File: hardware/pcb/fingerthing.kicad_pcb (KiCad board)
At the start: 2 copper layers, 52 x 51 mm, 43 parts, among them J1 10103594-0001LF, J2 TSW-118-07-L-D, J3 TSW-118-07-L-D, J4 SM03B-SRSS-TB(LF)(SN), SW1 434133025816, SW2 434133025816, U1 RP2350A, U2 NCP1117ST33T3G, U3 W25Q128JVSIQ, X1 12MHz

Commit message: usb / sensor layout
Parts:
- removed J3: TSW-118-07-L-D, RPI_COMPILED:samtec_tsw-118-07-l-d
- removed R4: 1k, RPI_COMPILED:generic_resc1005x35
- removed R9: 0, RPI_COMPILED:generic_resc1005x35
- removed SW2: 434133025816, RPI_COMPILED:wurthelek_434133025816
- added D1: green, LED_SMD:LED_0603_1608Metric, F.Cu at (30.0, 24.0)
- added R11: 5.1k, Resistor_SMD:R_0402_1005Metric, F.Cu at (10.5, 8.50)
- added R12: 5.1k, Resistor_SMD:R_0402_1005Metric, F.Cu at (23.5, 9.50)
- added R13: 1k, Resistor_SMD:R_0402_1005Metric, F.Cu at (30.0, 26.0)
- added R14: 10k, Resistor_SMD:R_0402_1005Metric, F.Cu at (10.0, 39.0)
- added SW3: 434133025816, RPI_COMPILED:wurthelek_434133025816, F.Cu at (10.0, 43.0)
- added U4: USBLC6-2SC6, Package_TO_SOT_SMD:SOT-23-6, F.Cu at (17.0, 11.0)
- J1: value 10103594-0001LF -> USB4105-GF-A; footprint RPI_COMPILED:amphenol_10103594-0001lf -> Connector_USB:USB_C_Receptacle_GCT_USB4105-xx-A_16P_TopMnt_Horizontal
- J2: value TSW-118-07-L-D -> R503; footprint RPI_COMPILED:samtec_tsw-118-07-l-d -> Connector_JST:JST_SH_SM06B-SRSS-TB_1x06-1MP_P1.00mm_Horizontal; moved to B.Cu
- J4: moved to B.Cu
- moved J4 112.5 mm to (25.5, 38.5), turned to 180 degrees
- moved MH3 111.0 mm to (30.5, 44.0)
- moved MH4 110.3 mm to (3.50, 44.0)
- moved C10 109.9 mm to (17.8, 34.9)
- moved C11 109.9 mm to (24.1, 27.4)
- moved C12 109.9 mm to (14.9, 20.6)
- moved C13 109.9 mm to (10.5, 24.6)
- moved C14 109.9 mm to (24.1, 28.4)
- moved C15 109.9 mm to (10.5, 29.4)
- moved C16 109.9 mm to (22.7, 32.0)
- moved C17 109.9 mm to (23.5, 25.0)
- moved C18 109.9 mm to (15.2, 34.1)
- moved C2 109.9 mm to (13.2, 10.8)
- moved C3 109.9 mm to (15.6, 37.0)
- moved C4 109.9 mm to (18.6, 37.0)
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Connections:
- net +1V1 renamed /+1V1
- net Net-(U1-USB_DM) renamed /USB_DM
- net Net-(U1-USB_DP) renamed /USB_DP
- C1 pad 1: VBUS -> /VBUS
- C1 pad 2: GND -> /GND
- C10 pad 2: GND -> /GND
- C11 pad 2: GND -> /GND
- C12 pad 1: +3V3 -> /+3V3
- C12 pad 2: GND -> /GND
- C13 pad 1: +3V3 -> /+3V3
- C13 pad 2: GND -> /GND
- C14 pad 1: +3V3 -> /+3V3
- C14 pad 2: GND -> /GND
- C15 pad 1: +3V3 -> /+3V3
- C15 pad 2: GND -> /GND
- C16 pad 1: +3V3 -> /+3V3
- C16 pad 2: GND -> /GND
- C17 pad 1: +3V3 -> /+3V3
- C17 pad 2: GND -> /GND
- C18 pad 1: +3V3 -> /+3V3
- C18 pad 2: GND -> /GND
- C19 pad 1: +3V3 -> /+3V3
- C19 pad 2: GND -> /GND
- C2 pad 1: +3V3 -> /+3V3
- C2 pad 2: GND -> /GND
- C3 pad 2: GND -> /GND
- C4 pad 2: GND -> /GND
- C5 pad 1: +3V3 -> /+3V3
- C5 pad 2: GND -> /GND
- C6 pad 1: +3V3 -> /+3V3
- C6 pad 2: GND -> /GND
- C7 pad 2: GND -> /GND
- C8 pad 2: GND -> /GND
- C9 pad 2: GND -> /GND
- J2 pad 1: GND -> /+3V3
- J2 pad 2: +3V3 -> /GND
- J2 pad 3: GND -> /GPIO5
- J2 pad 4: /GPIO0 -> /GPIO4
- J2 pad 5: GND -> /GPIO7
- J2 pad 6: /GPIO1 -> /+3V3
- J4 pad 2: GND -> /GND
- J4 pad 4: GND -> /GND
- J4 pad 5: GND -> /GND
- R1 pad 1: +3V3 -> /+3V3
- R3 pad 1: +3V3 -> /+3V3
- SW1 pad 1: GND -> /GND
- SW1 pad 2: GND -> /GND
- U1 pad 1: +3V3 -> /+3V3
- U1 pad 11: +3V3 -> /+3V3
- U1 pad 12: /GPIO8 -> unconnected-(U1-GPIO8-Pad12)
- U1 pad 13: /GPIO9 -> unconnected-(U1-GPIO9-Pad13)
- U1 pad 14: /GPIO10 -> unconnected-(U1-GPIO10-Pad14)
- U1 pad 15: /GPIO11 -> unconnected-(U1-GPIO11-Pad15)
- U1 pad 16: /GPIO12 -> unconnected-(U1-GPIO12-Pad16)
- U1 pad 17: /GPIO13 -> unconnected-(U1-GPIO13-Pad17)
- U1 pad 18: /GPIO14 -> unconnected-(U1-GPIO14-Pad18)
- U1 pad 19: /GPIO15 -> unconnected-(U1-GPIO15-Pad19)
- U1 pad 2: /GPIO0 -> unconnected-(U1-GPIO0-Pad2)
- U1 pad 20: +3V3 -> /+3V3
- U1 pad 26: /RUN -> unconnected-(U1-RUN-Pad26)
- U1 pad 27: /GPIO16 -> unconnected-(U1-GPIO16-Pad27)
- U1 pad 28: /GPIO17 -> unconnected-(U1-GPIO17-Pad28)
- U1 pad 29: /GPIO18 -> unconnected-(U1-GPIO18-Pad29)
- U1 pad 3: /GPIO1 -> unconnected-(U1-GPIO1-Pad3)
- U1 pad 30: +3V3 -> /+3V3
- U1 pad 31: /GPIO19 -> unconnected-(U1-GPIO19-Pad31)
- U1 pad 32: /GPIO20 -> unconnected-(U1-GPIO20-Pad32)
- U1 pad 33: /GPIO21 -> unconnected-(U1-GPIO21-Pad33)
- U1 pad 34: /GPIO22 -> unconnected-(U1-GPIO22-Pad34)
- U1 pad 35: /GPIO23 -> unconnected-(U1-GPIO23-Pad35)
- U1 pad 36: /GPIO24 -> unconnected-(U1-GPIO24-Pad36)
- U1 pad 38: +3V3 -> /+3V3
- U1 pad 4: /GPIO2 -> unconnected-(U1-GPIO2-Pad4)
- U1 pad 40: /GPIO26_ADC0 -> unconnected-(U1-GPIO26_ADC0-Pad40)
- U1 pad 41: /GPIO27_ADC1 -> unconnected-(U1-GPIO27_ADC1-Pad41)
- U1 pad 42: /GPIO28_ADC2 -> unconnected-(U1-GPIO28_ADC2-Pad42)
- U1 pad 43: /GPIO29_ADC3 -> unconnected-(U1-GPIO29_ADC3-Pad43)
- U1 pad 44: +3V3 -> /+3V3
- U1 pad 45: +3V3 -> /+3V3
- U1 pad 47: GND -> /GND
- U1 pad 49: +3V3 -> /+3V3
- U1 pad 5: /GPIO3 -> unconnected-(U1-GPIO3-Pad5)
- U1 pad 53: +3V3 -> /+3V3
- U1 pad 54: +3V3 -> /+3V3
- U1 pad 61: GND -> /GND
- U2 pad 1: GND -> /GND
- U2 pad 2: +3V3 -> /+3V3
- U2 pad 3: VBUS -> /VBUS
- U2 pad 4: +3V3 -> /+3V3
- U3 pad 4: GND -> /GND
- U3 pad 8: +3V3 -> /+3V3
- X1 pad 2: GND -> /GND
- X1 pad 4: GND -> /GND
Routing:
- net /GPIO0: track 39.0 -> 0.00 mm, vias 2 -> 0
- net +3V3: track 37.6 -> 0.00 mm, vias 2 -> 0
- net GND: track 37.5 -> 0.00 mm, vias 27 -> 0
- net /GPIO29_ADC3: track 33.6 -> 0.00 mm
- net /GPIO28_ADC2: track 31.9 -> 0.00 mm
- net /GPIO27_ADC1: track 30.3 -> 0.00 mm
- net /GPIO1: track 29.8 -> 0.00 mm
- net /GPIO26_ADC0: track 28.6 -> 0.00 mm
- net /GPIO2: track 28.2 -> 0.00 mm
- net /SWCLK: track 27.8 -> 0.00 mm
- net /GPIO25: track 27.7 -> 0.00 mm
- net /GPIO3: track 26.5 -> 0.00 mm
- net /GPIO24: track 26.1 -> 0.00 mm
- net /SWD: track 25.4 -> 0.00 mm
- net /GPIO15: track 25.2 -> 0.00 mm
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- added copper zone on F.Cu, net /+3V3
- added copper zone on F.Cu, net /GND
- removed copper zone on F.Cu, net +3V3
- removed copper zone on B.Cu, net GND
- removed copper zone on F.Cu, net GND
- removed copper zone on F.Cu, net VBUS
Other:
- board size 52 x 51 mm -> 34 x 48 mm
- copper layers 2 -> 4
- board text added: "CLK GND SWD"
- board text added: "fingerthing"
- board text removed: "3V3"
- board text removed: "ADC 26-29"
- board text removed: "BOOTSEL"
- board text removed: "DEBUG"
- board text removed: "GND"
- board text removed: "GP0"
- board text removed: "GP1"
- board text removed: "GP10"
- board text removed: "GP11"
- board text removed: "GP12"
- board text removed: "GP13"
- board text removed: "GP14"
- board text removed: "GP15"
- board text removed: "GP16"
- board text removed: "GP17"
- board text removed: "GP18"
- board text removed: "GP19"
- board text removed: "GP2"
- board text removed: "GP20"
- board text removed: "GP21"
- board text removed: "GP22"
- board text removed: "GP23"
- board text removed: "GP24"
- board text removed: "GP25"
- board text removed: "GP26"
- board text removed: "GP27"
- board text removed: "GP28"
- board text removed: "GP29"
- board text removed: "GP3"
- board text removed: "GP4"
- board text removed: "GP5"
- board text removed: "GP6"
- board text removed: "GP7"
- board text removed: "GP8"
- board text removed: "GP9"
- board text removed: "Minimal Design Example R4"
- board text removed: "Outer Row GND"
- board text removed: "RUN"
- board text removed: "Raspberry Pi RP2350A QFN-60"
- board text removed: "SWCLK"
- board text removed: "SWD"

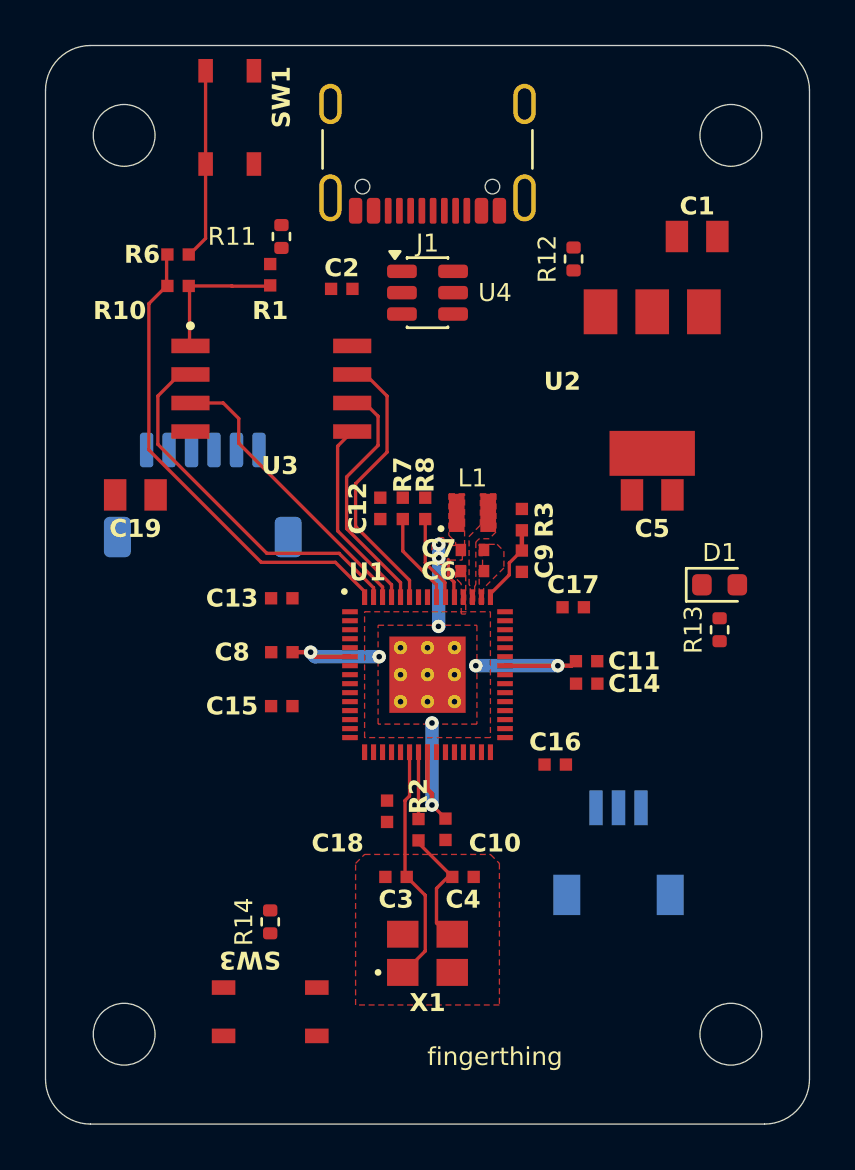
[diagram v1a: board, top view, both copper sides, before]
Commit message: pcb power / usb footprint
Ground and 3.3 V routing pass DRC clearance checks. ERC and schematic parity pass. 24 unconnected items remain.
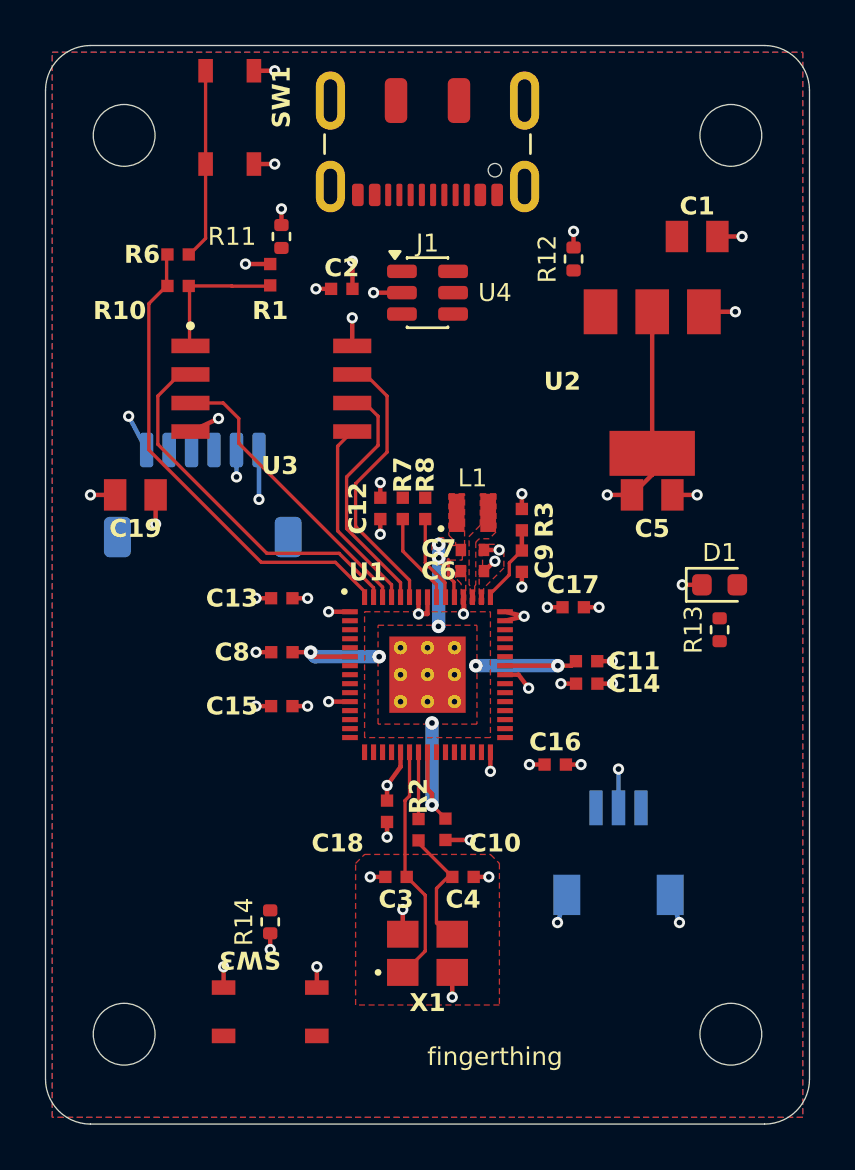
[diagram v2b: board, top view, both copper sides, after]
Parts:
- J1: value USB4105-GF-A -> DX07S016JA1R1500; footprint Connector_USB:USB_C_Receptacle_GCT_USB4105-xx-A_16P_TopMnt_Horizontal -> fingerthing:usb-c
- moved J1 0.07 mm to (17.0, 3.60)
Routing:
- net /+3V3: track 0.00 -> 35.4 mm, vias 0 -> 23
- net /GND: track 0.00 -> 32.5 mm, vias 0 -> 35
- added copper zone on In2.Cu, net /+3V3
- added copper zone on B.Cu, net /GND
- added copper zone on In1.Cu, net /GND

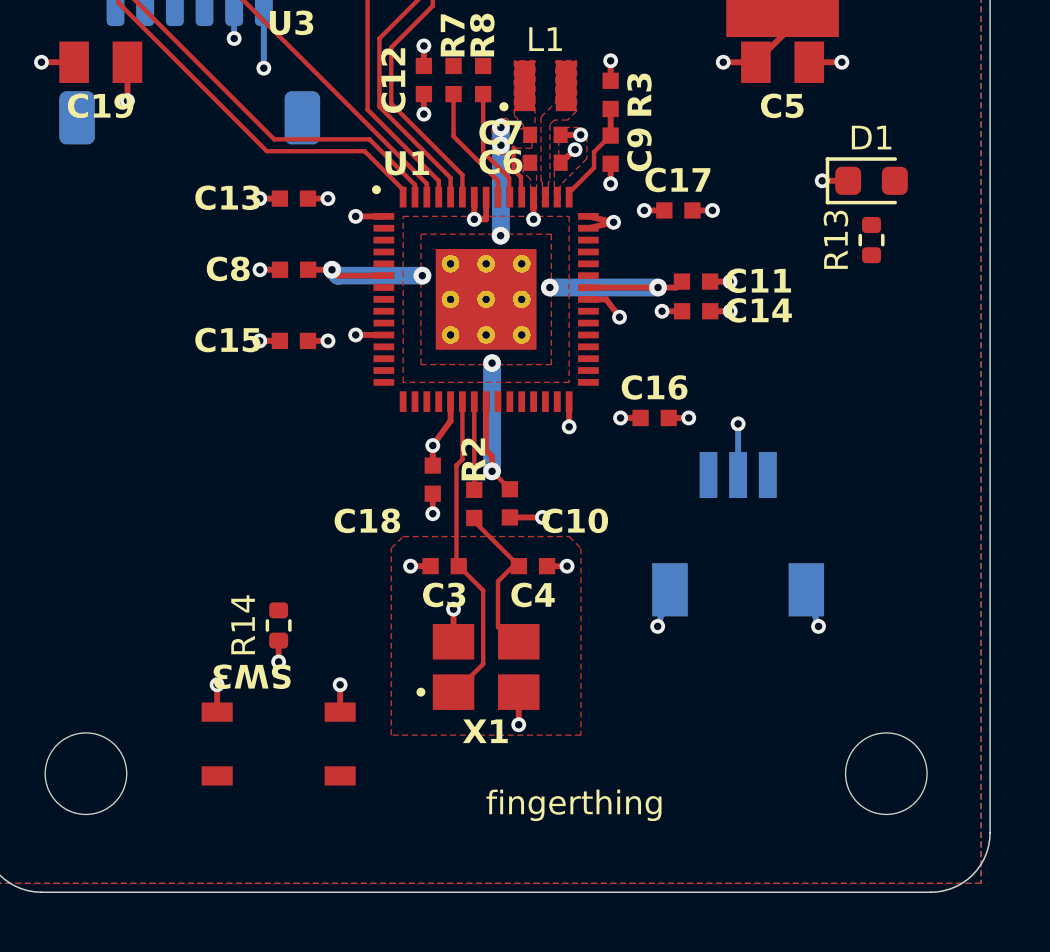
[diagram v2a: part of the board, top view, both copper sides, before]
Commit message: button / led routing
ERC and schematic parity pass. DRC has 19 unconnected items and no other violations. USB, sensor and SWD routing remain.
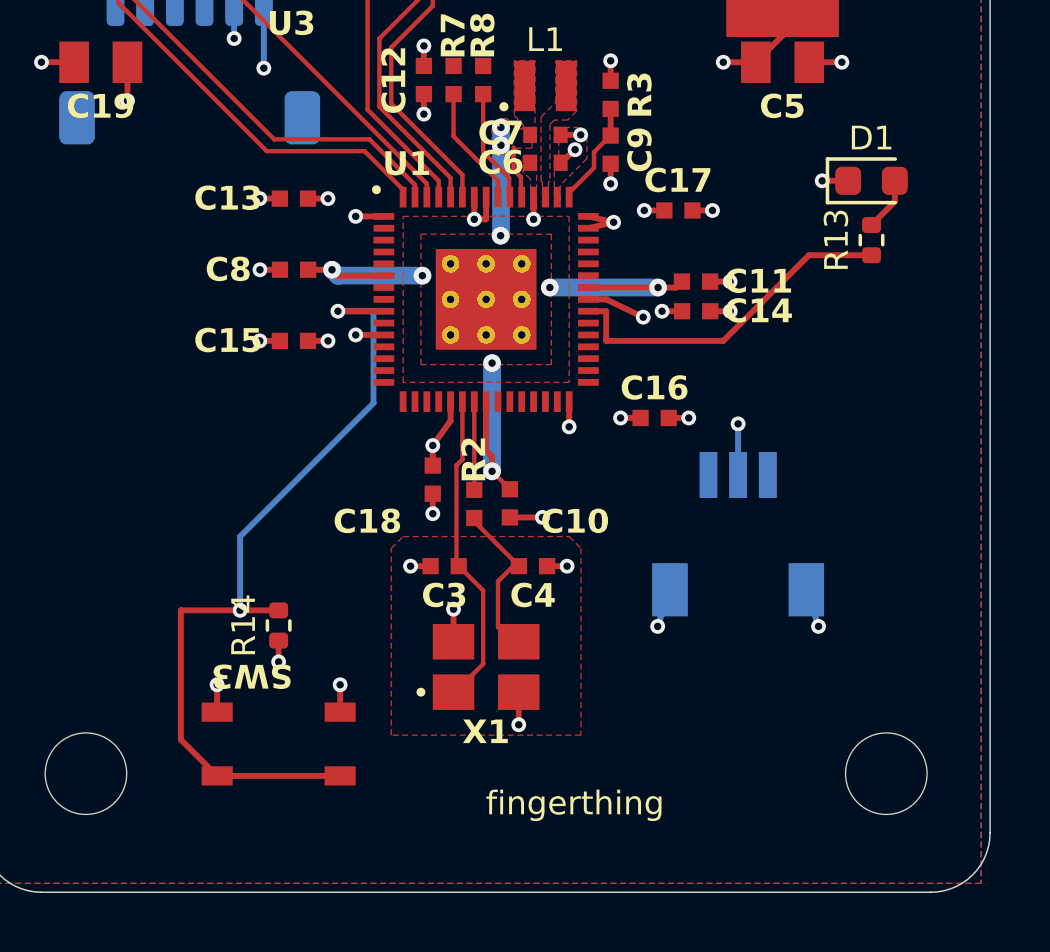
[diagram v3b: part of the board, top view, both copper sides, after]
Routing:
- net /GPIO6: track 0.00 -> 28.2 mm, vias 0 -> 2
- net /GPIO25: track 0.00 -> 11.7 mm
- net /LED_A: track 0.00 -> 1.82 mm
- net /+3V3: track 35.4 -> 36.1 mm
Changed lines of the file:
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@@
 	(segment
 		(start 21.05 28)
-		(end 21.5 28.6)
+		(end 22.3 28.6)
 		(width 0.2)
 		(layer "F.Cu")
@@
 	)
 	(via
-		(at 21.5 28.6)
+		(at 22.3 28.6)
 		(size 0.5)
 		(drill 0.25)
@@
 	)
 	(segment
+		(start 30 25.49)
+		(end 30.7875 24.7025)
+		(width 0.2)
+		(layer "F.Cu")
+		(net "/LED_A")
+	)
+	(segment
+		(start 30.7875 24.7025)
+		(end 30.7875 24)
+		(width 0.2)
+		(layer "F.Cu")
+		(net "/LED_A")
+	)
+	(segment
+		(start 21.05 29.4)
+		(end 25 29.4)
+		(width 0.2)
+		(layer "F.Cu")
+		(net "/GPIO25")
+	)
+	(segment
+		(start 20.45 28.4)
+		(end 21.05 28.4)
+		(width 0.2)
+		(layer "F.Cu")
+		(net "/GPIO25")
+	)
+	(segment
+		(start 21.05 28.4)
+		(end 21.05 29.4)
+		(width 0.2)
+		(layer "F.Cu")
+		(net "/GPIO25")
+	)
+	(segment
+		(start 27.89 26.51)
+		(end 30 26.51)
+		(width 0.2)
+		(layer "F.Cu")
+		(net "/GPIO25")
+	)
+	(segment
+		(start 25 29.4)
+		(end 27.89 26.51)
+		(width 0.2)
+		(layer "F.Cu")
+		(net "/GPIO25")
+	)
+	(segment
 		(start 7.125 5.25)
 		(end 7.125 1.125)
@@
 	)
 	(segment
+		(start 13.55 28.4)
+		(end 12 28.4)
+		(width 0.2)
+		(layer "F.Cu")
+		(net "/GPIO6")
+	)
+	(segment
+		(start 7.925 44.075)
+		(end 12.075 44.075)
+		(width 0.2)
+		(layer "F.Cu")
+		(net "/GPIO6")
+	)
+	(segment
+		(start 6.7 38.49)
+		(end 6.7 42.85)
+		(width 0.2)
+		(layer "F.Cu")
+		(net "/GPIO6")
+	)
+	(segment
+		(start 6.7 42.85)
+		(end 7.925 44.075)
+		(width 0.2)
+		(layer "F.Cu")
+		(net "/GPIO6")
+	)
+	(segment
+		(start 10 38.49)
+		(end 6.7 38.49)
+		(width 0.2)
+		(layer "F.Cu")
+		(net "/GPIO6")
+	)
+	(via
+		(at 8.7 38.49)
+		(size 0.5)
+		(drill 0.25)
+		(layers "F.Cu" "B.Cu")
+		(net "/GPIO6")
+	)
+	(via
+		(at 12 28.4)
+		(size 0.5)
+		(drill 0.25)
+		(layers "F.Cu" "B.Cu")
+		(net "/GPIO6")
+	)
+	(segment
+		(start 8.7 36)
+		(end 8.7 38.49)
+		(width 0.2)
+		(layer "B.Cu")
+		(net "/GPIO6")
+	)
+	(segment
+		(start 13.2 28.4)
+		(end 13.2 31.5)
+		(width 0.2)
+		(layer "B.Cu")
+		(net "/GPIO6")
+	)
+	(segment
+		(start 13.2 31.5)
+		(end 8.7 36)
+		(width 0.2)
+		(layer "B.Cu")
+		(net "/GPIO6")
+	)
+	(segment
+		(start 12 28.4)
+		(end 13.2 28.4)
+		(width 0.2)
+		(layer "B.Cu")
+		(net "/GPIO6")
+	)
+	(segment

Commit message: sensor / swd routing
The sensor signals use In2.Cu around the core regulator routing. A rear supply bridge reconnects the 3.3 V fill. ERC and schematic parity pass. DRC has 14 unconnected USB items and no other violations.
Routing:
- net /GPIO7: track 0.00 -> 16.2 mm, vias 0 -> 2
- net /SWCLK: track 0.00 -> 16.2 mm, vias 0 -> 1
- net /GPIO5: track 0.00 -> 15.4 mm, vias 0 -> 2
- net /GPIO4: track 0.00 -> 14.0 mm, vias 0 -> 2
- net /SWD: track 0.00 -> 8.16 mm, vias 0 -> 1
- net /+3V3: track 36.1 -> 41.4 mm

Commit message: usb power / cc routing
Connected both VBUS banks with 0.5 mm traces and routed separate CC pull-downs. ERC and schematic parity pass. Eight USB data connections remain, with no other DRC violations.
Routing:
- net /VBUS: track 0.00 -> 24.5 mm, vias 0 -> 4
- net /CC1: track 0.00 -> 14.4 mm, vias 0 -> 2
- net /CC2: track 0.00 -> 11.3 mm, vias 0 -> 2
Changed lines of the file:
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@@
+	)
+	(segment
+		(start 26.5 8.5)
+		(end 28.1 8.5)
+		(width 0.5)
+		(layer "F.Cu")
+		(net "/VBUS")
+	)
+	(segment
+		(start 19.35 6.65)
+		(end 19.35 7.9)
+		(width 0.5)
+		(layer "F.Cu")
+		(net "/VBUS")
+	)
+	(segment
+		(start 24.7 11.85)
+		(end 24.7 10.3)
+		(width 0.5)
+		(layer "F.Cu")
+		(net "/VBUS")
+	)
+	(segment
+		(start 18.1375 11)
+		(end 19.5 11)
+		(width 0.5)
+		(layer "F.Cu")
+		(net "/VBUS")
+	)
+	(segment
+		(start 24.7 10.3)
+		(end 26.5 8.5)
+		(width 0.5)
+		(layer "F.Cu")
+		(net "/VBUS")
+	)
+	(segment
+		(start 14.65 6.65)
+		(end 14.65 7.9)
+		(width 0.5)
+		(layer "F.Cu")
+		(net "/VBUS")
+	)
+	(via
+		(at 19.5 11)
+		(size 0.6)
+		(drill 0.3)
+		(layers "F.Cu" "B.Cu")
+		(net "/VBUS")
+	)
+	(via
+		(at 14.65 7.9)
+		(size 0.6)
+		(drill 0.3)
+		(layers "F.Cu" "B.Cu")
+		(net "/VBUS")
+	)
+	(via
+		(at 24.7 10.7)
+		(size 0.6)
+		(drill 0.3)
+		(layers "F.Cu" "B.Cu")
+		(net "/VBUS")
+	)
+	(via
+		(at 19.35 7.9)
+		(size 0.6)
+		(drill 0.3)
+		(layers "F.Cu" "B.Cu")
+		(net "/VBUS")
+	)
+	(segment
+		(start 19.35 7.9)
+		(end 20.15 8.7)
+		(width 0.5)
+		(layer "B.Cu")
+		(net "/VBUS")
+	)
+	(segment
+		(start 22.7 8.7)
+		(end 24.7 10.7)
+		(width 0.5)
+		(layer "B.Cu")
+		(net "/VBUS")
+	)
+	(segment
+		(start 19.5 9.35)
+		(end 20.15 8.7)
+		(width 0.5)
+		(layer "B.Cu")
+		(net "/VBUS")
+	)
+	(segment
+		(start 15.45 8.7)
+		(end 22.7 8.7)
+		(width 0.5)
+		(layer "B.Cu")
+		(net "/VBUS")
+	)
+	(segment
+		(start 19.5 11)
+		(end 19.5 9.35)
+		(width 0.5)
+		(layer "B.Cu")
+		(net "/VBUS")
+	)
+	(segment
+		(start 14.65 7.9)
+		(end 15.45 8.7)
+		(width 0.5)
+		(layer "B.Cu")
+		(net "/VBUS")
 	)
 	(segment
@@
 	)
 	(segment
+		(start 18.75 6.65)
+		(end 18.75 8.6)
+		(width 0.2)
+		(layer "F.Cu")
+		(net "/CC1")
+	)
+	(segment
+		(start 10.5 9.01)
+		(end 11.5 9.01)
+		(width 0.2)
+		(layer "F.Cu")
+		(net "/CC1")
+	)
+	(segment
+		(start 18.75 8.6)
+		(end 20.3 10.15)
+		(width 0.2)
+		(layer "F.Cu")
+		(net "/CC1")
+	)
+	(via
+		(at 20.3 10.15)
+		(size 0.5)
+		(drill 0.25)
+		(layers "F.Cu" "B.Cu")
+		(net "/CC1")
+	)
+	(via
+		(at 11.5 9.01)
+		(size 0.5)
+		(drill 0.25)
+		(layers "F.Cu" "B.Cu")
+		(net "/CC1")
+	)
+	(segment
+		(start 19.16 9.01)
+		(end 11.5 9.01)
+		(width 0.2)
+		(layer "In2.Cu")
+		(net "/CC1")
+	)
+	(segment
+		(start 20.3 10.15)
+		(end 19.16 9.01)
+		(width 0.2)
+		(layer "In2.Cu")
+		(net "/CC1")
+	)
+	(segment
+		(start 15.75 6.65)
+		(end 15.75 7.7)
+		(width 0.2)
+		(layer "F.Cu")
+		(net "/CC2")
+	)
+	(segment
+		(start 23.5 10.01)
+		(end 22.3 10.01)
+		(width 0.2)
+		(layer "F.Cu")
+		(net "/CC2")
+	)
+	(via
+		(at 15.75 7.7)
+		(size 0.5)
+		(drill 0.25)
+		(layers "F.Cu" "B.Cu")
+		(net "/CC2")
+	)
+	(via
+		(at 22.3 10.01)
+		(size 0.5)
+		(drill 0.25)
+		(layers "F.Cu" "B.Cu")
+		(net "/CC2")
+	)
+	(segment
+		(start 22.3 8.8)
+		(end 22.3 10.01)
+		(width 0.2)
+		(layer "In2.Cu")
+		(net "/CC2")
+	)
+	(segment
+		(start 20.3 7.5)
+		(end 21.6 8.8)
+		(width 0.2)
+		(layer "In2.Cu")
+		(net "/CC2")
+	)
+	(segment
+		(start 17 7.7)
+		(end 17.7 7)
+		(width 0.2)
+		(layer "In2.Cu")
+		(net "/CC2")
+	)
+	(segment
+		(start 20.3 7)
+		(end 20.3 7.5)
+		(width 0.2)
+		(layer "In2.Cu")
+		(net "/CC2")
+	)
+	(segment
+		(start 15.75 7.7)
+		(end 17 7.7)
+		(width 0.2)
+		(layer "In2.Cu")
+		(net "/CC2")
+	)
+	(segment
+		(start 17.7 7)
+		(end 20.3 7)
+		(width 0.2)
+		(layer "In2.Cu")
+		(net "/CC2")
+	)
+	(segment
+		(start 21.6 8.8)
+		(end 22.3 8.8)
+		(width 0.2)
+		(layer "In2.Cu")
+		(net "/CC2")
+	)
+	(segment
